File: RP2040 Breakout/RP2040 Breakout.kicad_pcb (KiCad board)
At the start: 6 copper layers, 38.1 x 43.2 mm, 46 parts, among them J1 USB_C_Receptacle_USB2.0, J3 Conn_01x16_Pin, J5 Conn_01x16_Pin, SW1 ~{RST}, SW2 BTSEL, SW3 SLEEP, U1 RP2040, U3 W25Q128JVS, U4 LP2980IM5X-3.3, X1 ABM8G-12.000MHZ-B4Y-T

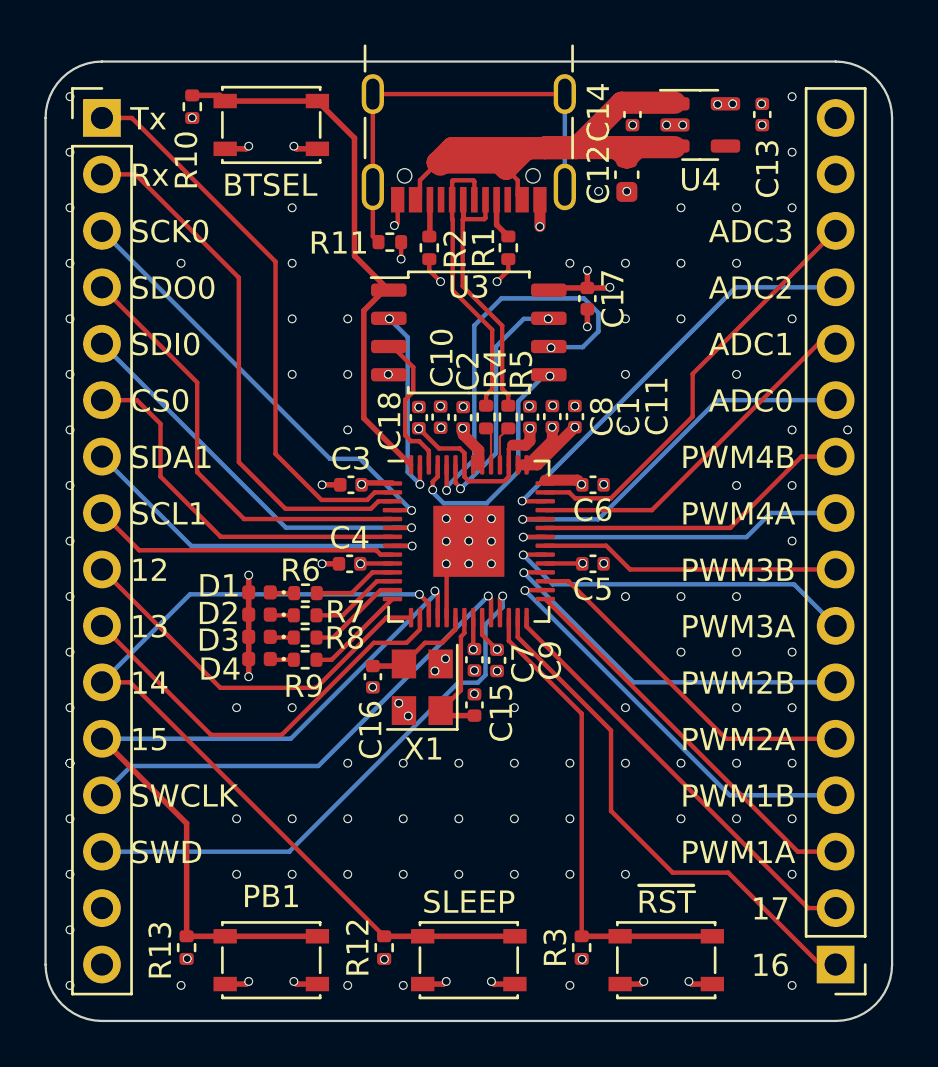
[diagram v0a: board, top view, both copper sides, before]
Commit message: Cleaned up schematic a bit and rerouted buttons.
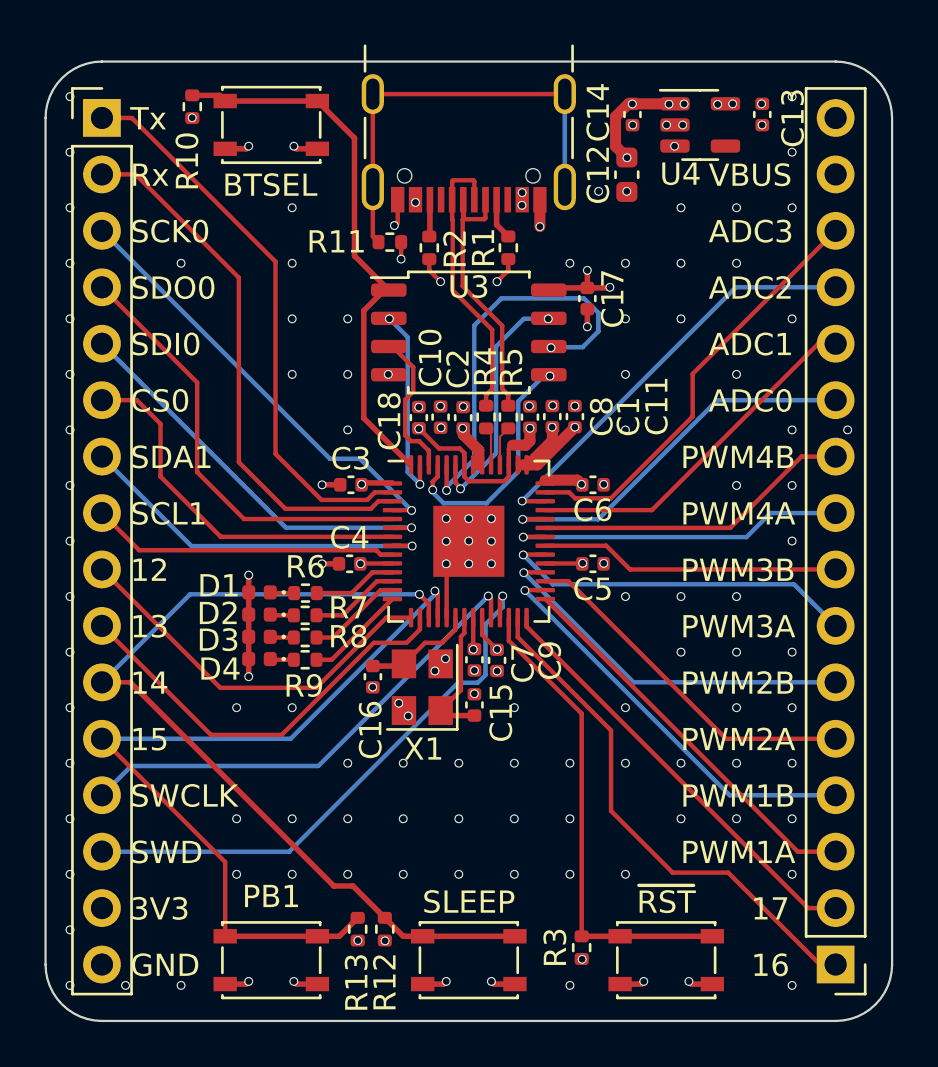
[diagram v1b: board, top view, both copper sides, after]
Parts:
- moved R13 7.74 mm to (103.0, 97.5)
- moved R12 0.83 mm to (104.2, 97.5)
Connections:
- J5 pad 15: +3V3 -> +5V
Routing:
- net +5V: track 35.3 -> 5.39 mm, vias 0 -> 8
- net /GPIO15: track 35.4 -> 36.6 mm
- net GND: vias 139 -> 137
- added copper zone on In3.Cu, net +5V
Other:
- board text added: "3V3"
- board text added: "GND"
- board text added: "VBUS"

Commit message: Add QR code to github page.
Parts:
- added QR*****: QRCODE_httpsgithub.comTobiMcKellarRP2040Breakout, images:QRCODE_httpsgithub.comTobiMcKellarRP2040Breakout, B.Cu at (108.0, 80.0)
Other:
- board text added: "RP2040 Breakout V1.0 03/06/24 By T. McKellar"
